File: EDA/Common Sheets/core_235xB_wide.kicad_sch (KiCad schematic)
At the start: 32 parts, among them J4 SM03B-SRSS-TB, J4.1 Conn_01x04, J6 Conn_01x02, SW1 SW_DIP_x04, U1 RP2350_60QFN, U2 W25Q128JVS, Y1 12MHz

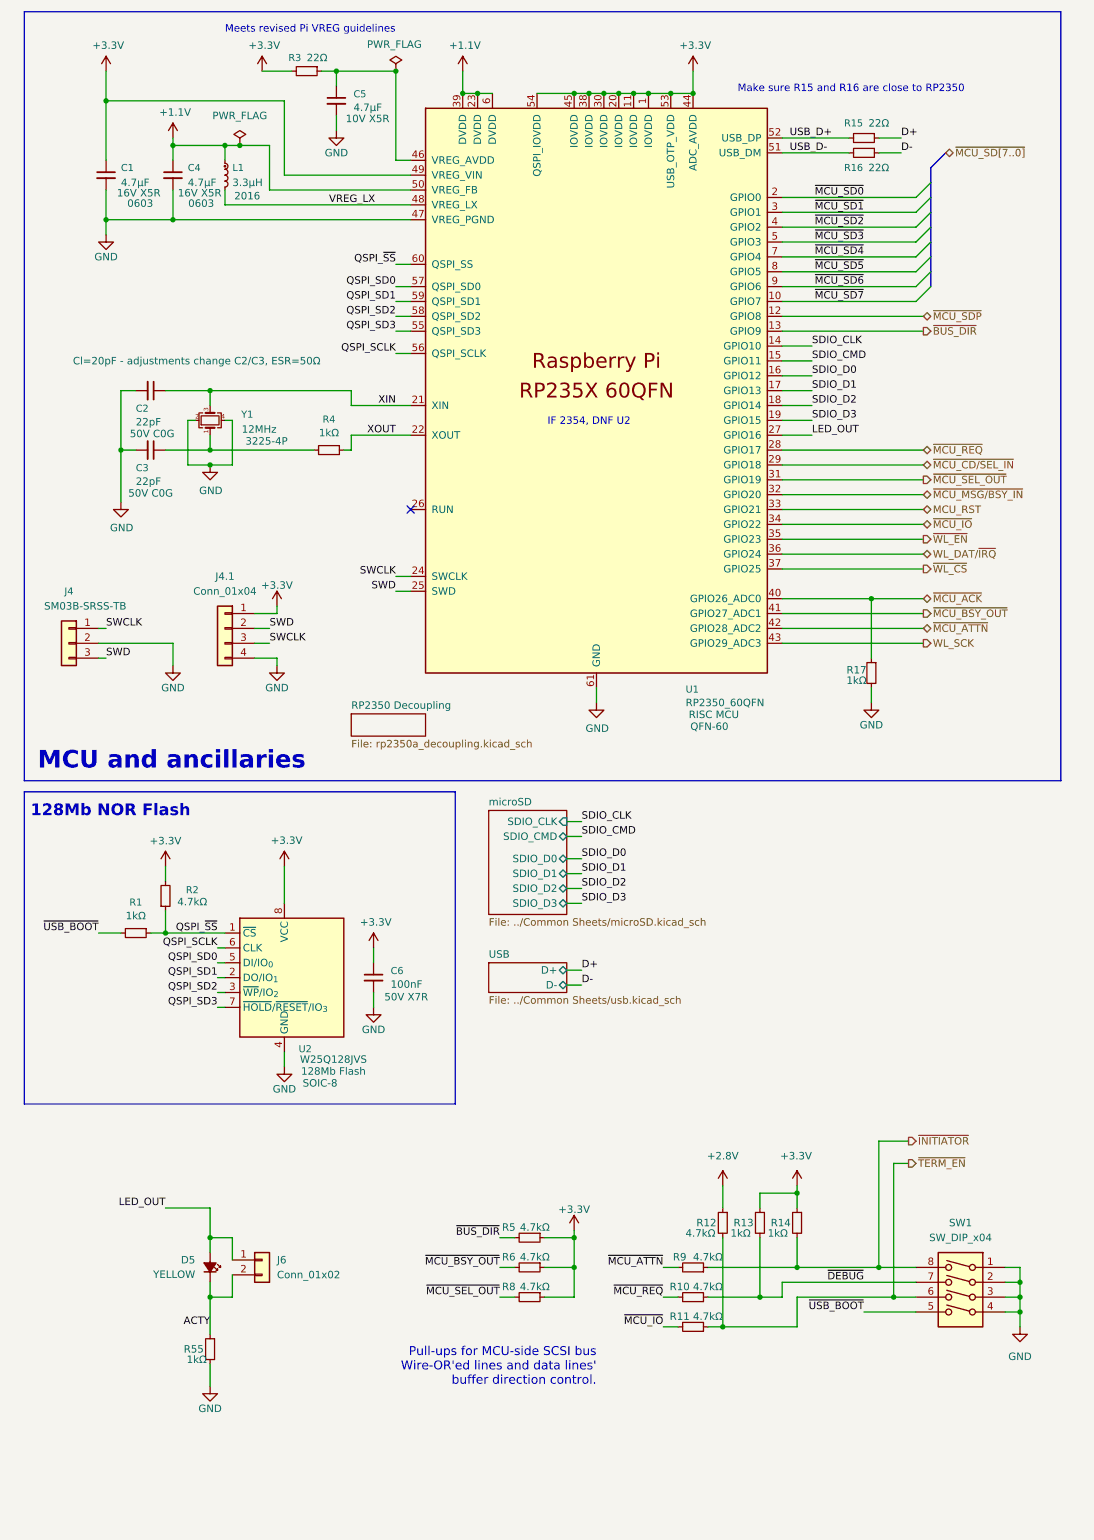
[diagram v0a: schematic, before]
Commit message: Started work on thru-hole SCA wide variant
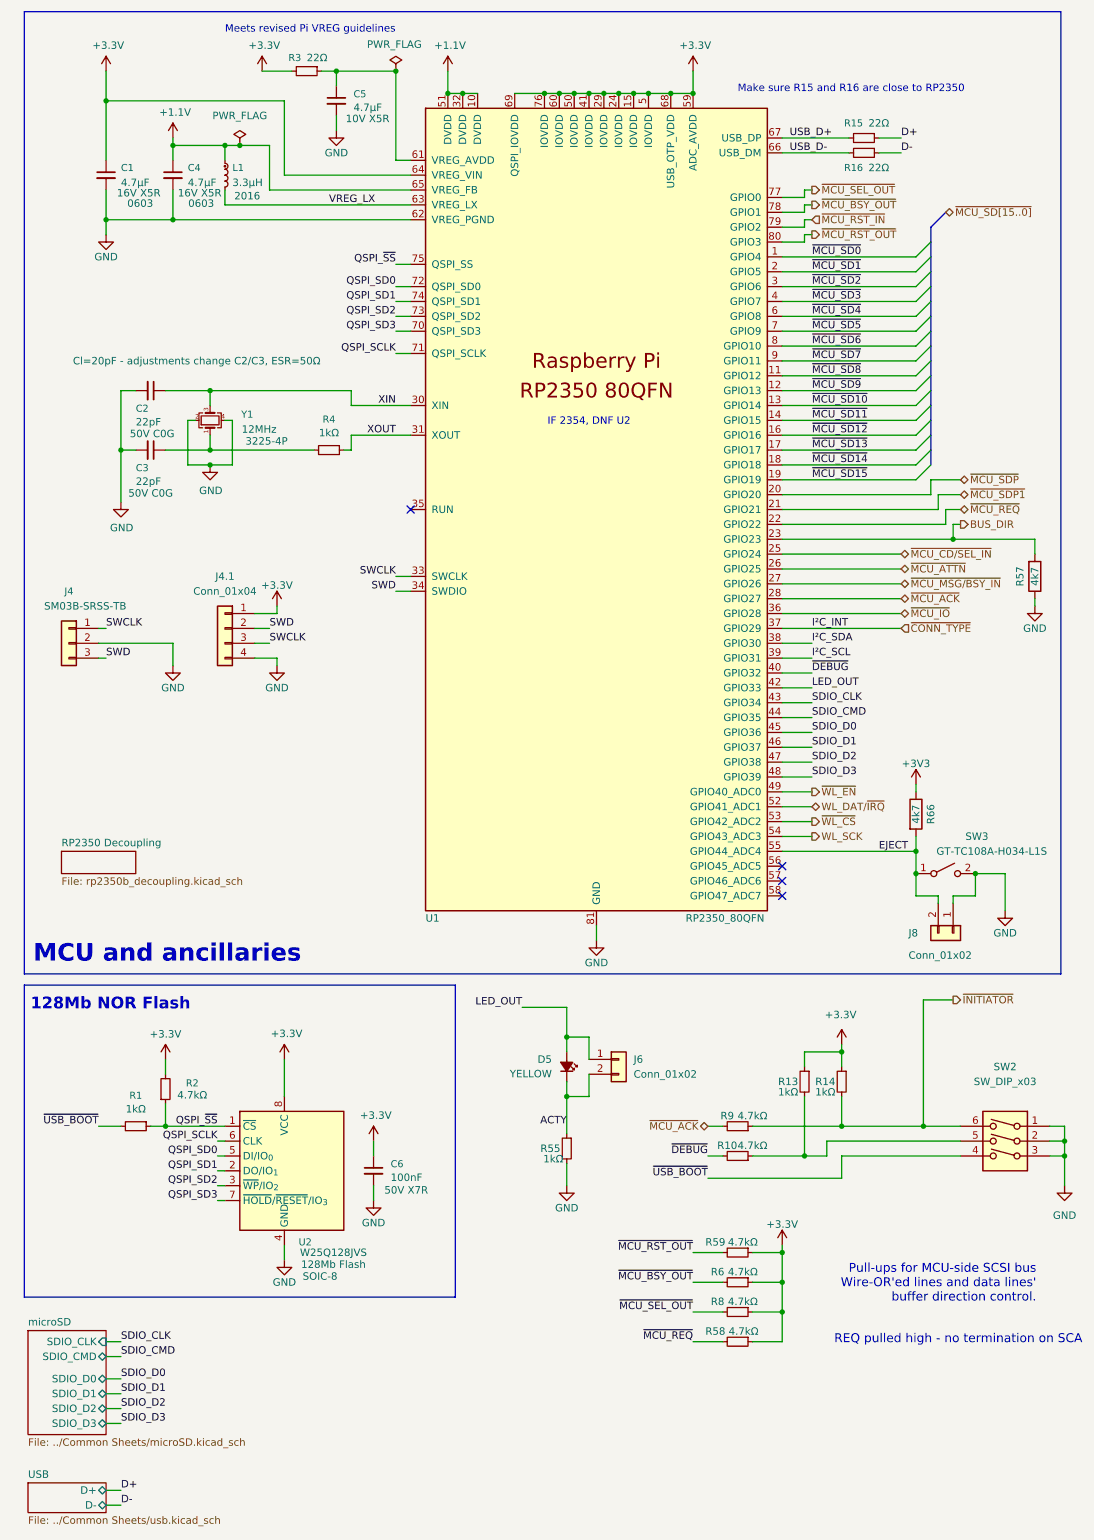
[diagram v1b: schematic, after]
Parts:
- removed R11, R12, R5: 4.7kΩ, Resistor_SMD:R_0603_1608Metric, symbol Device:R_Small
- removed R17: 1kΩ, Resistor_SMD:R_0603_1608Metric, symbol Device:R_Small
- removed SW1: SW_DIP_x04, Button_Switch_SMD:SW_DIP_SPSTx04_Slide_6.7x11.72mm_W8.61mm_P2.54mm_LowProfile, symbol Switch:SW_DIP_x04
- removed U1: RP2350_60QFN, Package_DFN_QFN:QFN-60-1EP_7x7mm_P0.4mm_EP3.4x3.4mm_ThermalVias, symbol GBSCSI:RP2350_60QFN
- added J8: Conn_01x02, Connector_PinHeader_2.54mm:PinHeader_1x02_P2.54mm_Vertical, symbol Connector_Generic:Conn_01x02
- added R57, R66: 4k7, Resistor_SMD:R_0603_1608Metric, symbol Device:R
- added R58, R59: 4.7kΩ, Resistor_SMD:R_0603_1608Metric, symbol Device:R_Small
- added SW2: SW_DIP_x03, Button_Switch_SMD:SW_DIP_SPSTx03_Slide_6.7x9.18mm_W8.61mm_P2.54mm_LowProfile, symbol Switch:SW_DIP_x03
- added SW3: GT-TC108A-H034-L1S, GBSCSI:SW_Push_1P1T-MP_NO_Horizontal_Alps_SKRTLAE010, symbol Switch:SW_SPST
- added U1: RP2350_80QFN, GBSCSI:RP2350-QFN-80-1EP_10x10_P0.4mm_EP3.4x3.4mm_ThermalVias, symbol GBSCSI:RP2350_80QFN
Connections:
- net +1.1V: now also U1.10 (DVDD), U1.32 (DVDD), U1.51 (DVDD), U1.65 (VREG_FB)
- net +3.3V: now also R58.1, R59.1, U1.15 (IOVDD), U1.24 (IOVDD), U1.29 (IOVDD), U1.41 (IOVDD), U1.5 (IOVDD), U1.50 (IOVDD), U1.59 (ADC_AVDD), U1.60 (IOVDD), U1.64 (VREG_VIN), U1.68 (USB_OTP_VDD), U1.69 (QSPI_IOVDD), U1.76 (IOVDD)
- net GND: now also J8.1 (Pin_1), R57.1, SW2.1, SW2.2, SW2.3, SW3.2 (B), U1.62 (VREG_PGND), U1.81 (GND)
- net LED_OUT: now also U1.42 (GPIO33)
- net QSPI_SCLK: now also U1.71 (QSPI_SCLK)
- net QSPI_SD0: now also U1.72 (QSPI_SD0)
- net QSPI_SD1: now also U1.74 (QSPI_SD1)
- net QSPI_SD2: now also U1.73 (QSPI_SD2)
- net QSPI_SD3: now also U1.70 (QSPI_SD3)
- net QSPI_~{SS}: now also U1.75 (QSPI_SS)
- net SDIO_CLK: now also U1.43 (GPIO34)
- net SDIO_CMD: now also U1.44 (GPIO35)
- net SDIO_D0: now also U1.45 (GPIO36)
- net SDIO_D1: now also U1.46 (GPIO37)
- net SDIO_D2: now also U1.47 (GPIO38)
- net SDIO_D3: now also U1.48 (GPIO39)
- net SWCLK: now also U1.33 (SWCLK)
- net SWD: now also U1.34 (SWDIO)
- net USB_D+: now also U1.67 (USB_DP)
- net USB_D-: now also U1.66 (USB_DM)
- net VREG_LX: now also U1.63 (VREG_LX)
- net WL_DAT/~{IRQ}: now also U1.52 (GPIO41_ADC1)
- net WL_SCK: now also U1.54 (GPIO43_ADC3)
- net XIN: now also U1.30 (XIN)
- net XOUT: now also U1.31 (XOUT)
- net ~{DEBUG}: now also R10.2, U1.40 (GPIO32); no longer R10.1, R13.2
- net ~{INITIATOR}: now also SW2.6
- net ~{MCU_ACK}: now also R9.2, U1.28 (GPIO27)
- net ~{MCU_ATTN}: now also U1.26 (GPIO25); no longer R9.2
- net ~{MCU_BSY_OUT}: now also U1.78 (GPIO1)
- net ~{MCU_CD/SEL_IN}: now also U1.25 (GPIO24)
- net ~{MCU_IO}: now also U1.36 (GPIO28)
- net ~{MCU_MSG/BSY_IN}: now also U1.27 (GPIO26)
- net ~{MCU_REQ}: now also R58.2, U1.22 (GPIO22); no longer R10.2
- net ~{MCU_SD0}: now also U1.1 (GPIO4)
- net ~{MCU_SD1}: now also U1.2 (GPIO5)
- net ~{MCU_SD2}: now also U1.3 (GPIO6)
- net ~{MCU_SD3}: now also U1.4 (GPIO7)
- net ~{MCU_SD4}: now also U1.6 (GPIO8)
- net ~{MCU_SD5}: now also U1.7 (GPIO9)
- net ~{MCU_SD6}: now also U1.8 (GPIO10)
- net ~{MCU_SD7}: now also U1.9 (GPIO11)
- net ~{MCU_SDP}: now also U1.20 (GPIO20)
- net ~{MCU_SEL_OUT}: now also U1.77 (GPIO0)
- net ~{USB_BOOT}: now also SW2.4
- net ~{WL_CS}: now also U1.53 (GPIO42_ADC2)
- net ~{WL_EN}: now also U1.49 (GPIO40_ADC0)
- net at C5.1, R3.1: now also U1.61 (VREG_AVDD)
- new net: R10.1, R13.2, SW2.5
- new net +3V3: R66.1
- new net BUS_DIR: R57.2, U1.23 (GPIO23)
- new net EJECT: J8.2 (Pin_2), R66.2, SW3.1 (A), U1.55 (GPIO44_ADC4)
- new net I²C_SCL: U1.39 (GPIO31)
- new net I²C_SDA: U1.38 (GPIO30)
- new net ~{CONN_TYPE}: U1.37 (GPIO29)
- new net ~{MCU_RST_IN}: U1.79 (GPIO2)
- new net ~{MCU_RST_OUT}: R59.2, U1.80 (GPIO3)
- new net ~{MCU_SD10}: U1.13 (GPIO14)
- new net ~{MCU_SD11}: U1.14 (GPIO15)
- new net ~{MCU_SD12}: U1.16 (GPIO16)
- new net ~{MCU_SD13}: U1.17 (GPIO17)
- new net ~{MCU_SD14}: U1.18 (GPIO18)
- new net ~{MCU_SD15}: U1.19 (GPIO19)
- new net ~{MCU_SD8}: U1.11 (GPIO12)
- new net ~{MCU_SD9}: U1.12 (GPIO13)
- new net ~{MCU_SDP1}: U1.21 (GPIO21)
- no-connect marks 1 -> 4
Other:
- sheet RP2350 Decoupling: file rp2350a_decoupling.kicad_sch -> rp2350b_decoupling.kicad_sch
- note added: "REQ pulled high - no termination on SCA"
- moved on the sheet: C6, D5, J6, R1, R10, R13, R14, R2, R55, R6, R8, R9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

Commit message: Fixing up schematics for SCA before layout
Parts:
- R57, R66: value 4k7 -> 4.7kΩ
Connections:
- net +3V3 is gone; now on net +3.3V: R66.1
- net ~{CONN_TYPE} renamed I²C_INT
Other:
- title: GBSCSI2 Common Platform Core - RP235xA, Narrow -> GBSCSI2 Common Platform Core - RP235xB, Wide
- moved on the sheet: R57
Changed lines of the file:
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@@
 	(paper "A4" portrait)
 	(title_block
-		(title "GBSCSI2 Common Platform Core - RP235xA, Narrow")
+		(title "GBSCSI2 Common Platform Core - RP235xB, Wide")
 		(date "2026-02-01")
 		(rev "2.0")
@@
 	(wire
 		(pts
-			(xy 173.99 105.41) (xy 187.96 105.41)
+			(xy 173.99 105.41) (xy 185.42 105.41)
 		)
 		(stroke
@@
 	(wire
 		(pts
-			(xy 149.86 125.73) (xy 144.78 125.73)
+			(xy 165.1 125.73) (xy 144.78 125.73)
 		)
 		(stroke
@@
 	(wire
 		(pts
-			(xy 187.96 116.84) (xy 187.96 115.57)
+			(xy 185.42 116.84) (xy 185.42 115.57)
 		)
 		(stroke
@@
 	(wire
 		(pts
-			(xy 29.21 50.8) (xy 29.21 53.34)
+			(xy 29.21 50.8) (xy 29.21 54.61)
 		)
 		(stroke
@@
 	(wire
 		(pts
-			(xy 187.96 105.41) (xy 187.96 107.95)
+			(xy 185.42 105.41) (xy 185.42 107.95)
 		)
 		(stroke
@@
 	(wire
 		(pts
-			(xy 149.86 123.19) (xy 144.78 123.19)
+			(xy 165.1 123.19) (xy 144.78 123.19)
 		)
 		(stroke
@@
 		)
 	)
-	(label "I²C_INT"
-		(at 149.86 120.65 0)
-		(effects
-			(font
-				(size 1.27 1.27)
-			)
-			(justify left bottom)
-		)
-	)
 	(label "SWCLK"
 		(at 29.21 120.65 0)
@@
 		)
 	)
-	(label "I²C_SDA"
-		(at 149.86 123.19 0)
-		(effects
-			(font
-				(size 1.27 1.27)
-			)
-			(justify left bottom)
-		)
-	)
 	(label "D+"
 		(at 31.75 267.97 0)
@@
 		)
 	)
-	(label "I²C_SCL"
-		(at 149.86 125.73 0)
-		(effects
-			(font
-				(size 1.27 1.27)
-			)
-			(justify left bottom)
-		)
-	)
 	(label "SWD"
 		(at 57.15 120.65 0)
@@
 		)
 	)
+	(hierarchical_label "I²C_INT"
+		(shape input)
+		(at 165.1 120.65 0)
+		(effects
+			(font
+				(size 1.27 1.27)
+			)
+			(justify left)
+		)
+	)
 	(hierarchical_label "~{MCU_BSY_OUT}"
 		(shape output)
@@
 		)
 	)
-	(hierarchical_label "WL_SCK"
+	(hierarchical_label "I²C_SCL"
 		(shape output)
-		(at 149.86 156.21 0)
+		(at 165.1 125.73 0)
 		(effects
 			(font
@@
 		)
 	)
-	(hierarchical_label "~{CONN_TYPE}"
-		(shape input)
-		(at 165.1 120.65 0)
+	(hierarchical_label "WL_SCK"
+		(shape output)
+		(at 149.86 156.21 0)
 		(effects
 			(font
@@
 		)
 	)
+	(hierarchical_label "I²C_SDA"
+		(shape bidirectional)
+		(at 165.1 123.19 0)
+		(effects
+			(font
+				(size 1.27 1.27)
+			)
+			(justify left)
+		)
+	)
 	(hierarchical_label "~{MCU_SD[15..0]}"
 		(shape bidirectional)
@@
 		(dnp no)
 		(property "Reference" "R55"
-			(at 105.156 209.55 0)
+			(at 104.902 209.55 0)
 			(effects
 				(font
@@
 		)
 		(property "Value" "1kΩ"
-			(at 105.664 211.328 0)
+			(at 104.902 211.328 0)
 			(effects
 				(font
@@
 	(symbol
 		(lib_id "power:GND")
-		(at 29.21 53.34 0)
+		(at 29.21 54.61 0)
 		(mirror y)
 		(unit 1)
@@
 		(dnp no)
 		(property "Reference" "#PWR02"
-			(at 29.21 59.69 0)
+			(at 29.21 60.96 0)
 			(effects
 				(font
@@
 		)
 		(property "Value" "GND"
-			(at 29.21 57.15 0)
+			(at 29.21 58.42 0)
 			(effects
 				(font
@@
 		)
 		(property "Footprint" ""
-			(at 29.21 53.34 0)
+			(at 29.21 54.61 0)
 			(effects
 				(font
@@
 		)
 		(property "Datasheet" ""
-			(at 29.21 53.34 0)
+			(at 29.21 54.61 0)
 			(effects
 				(font
@@
 		)
 		(property "Description" ""
-			(at 29.21 53.34 0)
+			(at 29.21 54.61 0)
 			(effects
 				(font
@@
 		(dnp no)
 		(property "Reference" "R66"
-			(at 170.18 152.4 90)
+			(at 171.958 151.13 0)
 			(effects
 				(font
@@
 			)
 		)
-		(property "Value" "4k7"
-			(at 167.64 152.4 90)
+		(property "Value" "4.7kΩ"
+			(at 171.958 153.67 0)
 			(effects
 				(font
@@
 			)
 		)
-		(property "Value" "+3V3"
-			(at 167.64 143.764 0)
+		(property "Value" "+3.3V"
+			(at 167.64 142.24 0)
 			(effects
 				(font
@@
 	(symbol
 		(lib_id "Device:R")
-		(at 187.96 111.76 0)
+		(at 185.42 111.76 0)
 		(mirror x)
 		(unit 1)
@@
 		(dnp no)
 		(property "Reference" "R57"
-			(at 185.42 111.76 90)
+			(at 189.484 110.998 0)
 			(effects
 				(font
@@
 			)
 		)
-		(property "Value" "4k7"
-			(at 187.96 111.76 90)
+		(property "Value" "4.7kΩ"
+			(at 189.484 113.538 0)
 			(effects
 				(font
@@
 		)
 		(property "Footprint" "Resistor_SMD:R_0603_1608Metric"
-			(at 186.182 111.76 90)
+			(at 183.642 111.76 90)
 			(effects
 				(font
@@
 		)
 		(property "Datasheet" ""
-			(at 187.96 111.76 0)
+			(at 185.42 111.76 0)
 			(effects
 				(font
@@
 		)
 		(property "Description" ""
-			(at 187.96 111.76 0)
+			(at 185.42 111.76 0)
 			(effects
 				(font
@@
 		)
 		(property "LCSC" "C23162"
-			(at 187.96 111.76 0)
+			(at 185.42 111.76 0)
 			(effects
 				(font
@@
 		)
 		(property "LCSC Part #" "C23162"
-			(at 187.96 111.76 0)
+			(at 185.42 111.76 0)
 			(effects
 				(font
@@
 	(symbol
 		(lib_id "power:GND")
-		(at 187.96 116.84 0)
+		(at 185.42 116.84 0)
 		(mirror y)
 		(unit 1)
@@
 		(dnp no)
 		(property "Reference" "#PWR025"
-			(at 187.96 123.19 0)
+			(at 185.42 123.19 0)
 			(effects
 				(font
@@
 		)
 		(property "Value" "GND"
-			(at 187.96 120.65 0)
+			(at 185.42 120.65 0)
 			(effects
 				(font
@@
 		)
 		(property "Footprint" ""
-			(at 187.96 116.84 0)
+			(at 185.42 116.84 0)
 			(effects
 				(font
@@
 		)
 		(property "Datasheet" ""
-			(at 187.96 116.84 0)
+			(at 185.42 116.84 0)
 			(effects
 				(font
@@
 		)
 		(property "Description" ""
-			(at 187.96 116.84 0)
+			(at 185.42 116.84 0)
 			(effects
 				(font

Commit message: SCA variant mostly laid out
Or rather, a first pass.
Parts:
- SW3: footprint GBSCSI:SW_Push_1P1T-MP_NO_Horizontal_Alps_SKRTLAE010 -> Button_Switch_SMD:SW_Push_1P1T-MP_NO_Horizontal_Alps_SKRTLAE010
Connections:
- net +3.3V: no longer R58.1, R59.1, R6.1, R8.1
- new net +2.8V: R58.1, R59.1, R6.1, R8.1
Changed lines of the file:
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@@
 			)
 		)
-		(property "Footprint" "GBSCSI:SW_Push_1P1T-MP_NO_Horizontal_Alps_SKRTLAE010"
+		(property "Footprint" "Button_Switch_SMD:SW_Push_1P1T-MP_NO_Horizontal_Alps_SKRTLAE010"
 			(at 172.72 162.56 0)
 			(effects
@@
 	)
 	(symbol
+		(lib_id "power:+2V8")
+		(at 144.78 226.06 0)
+		(unit 1)
+		(exclude_from_sim no)
+		(in_bom yes)
+		(on_board yes)
+		(dnp no)
+		(fields_autoplaced yes)
+		(property "Reference" "#PWR017"
+			(at 144.78 229.87 0)
+			(effects
+				(font
+					(size 1.27 1.27)
+				)
+				(hide yes)
+			)
+		)
+		(property "Value" "+2.8V"
+			(at 144.78 220.98 0)
+			(effects
+				(font
+					(size 1.27 1.27)
+				)
+			)
+		)
+		(property "Footprint" ""
+			(at 144.78 226.06 0)
+			(effects
+				(font
+					(size 1.27 1.27)
+				)
+				(hide yes)
+			)
+		)
+		(property "Datasheet" ""
+			(at 144.78 226.06 0)
+			(effects
+				(font
+					(size 1.27 1.27)
+				)
+				(hide yes)
+			)
+		)
+		(property "Description" ""
+			(at 144.78 226.06 0)
+			(effects
+				(font
+					(size 1.27 1.27)
+				)
+				(hide yes)
+			)
+		)
+		(pin "1"
+		)
+		(instances
+			(project "GBSCSI2_2.5SCA_TH_235x"
+				(path "/93ed3756-682c-4bf3-aa83-42c6b59d82c2/871f9ffd-aa9f-4db2-af7f-735335bcb730"
+					(reference "#PWR017")
+					(unit 1)
+				)
+			)
+		)
+	)
+	(symbol
 		(lib_id "Device:C_Small")
 		(at 40.64 43.18 0)
@@
 					(unit 1)
 				)
-			)
-		)
-	)
-	(symbol
-		(lib_id "power:+3.3V")
-		(at 144.78 226.06 0)
-		(mirror y)
-		(unit 1)
-		(exclude_from_sim no)
-		(in_bom yes)
-		(on_board yes)
-		(dnp no)
-		(property "Reference" "#PWR017"
-			(at 144.78 229.87 0)
-			(effects
-				(font
-					(size 1.27 1.27)
-				)
-				(hide yes)
-			)
-		)
-		(property "Value" "+3.3V"
-			(at 144.78 222.504 0)
-			(effects
-				(font
-					(size 1.27 1.27)
-				)
-			)
-		)
-		(property "Footprint" ""
-			(at 144.78 226.06 0)
-			(effects
-				(font
-					(size 1.27 1.27)
-				)
-				(hide yes)
-			)
-		)
-		(property "Datasheet" ""
-			(at 144.78 226.06 0)
-			(effects
-				(font
-					(size 1.27 1.27)
-				)
-				(hide yes)
-			)
-		)
-		(property "Description" "Power symbol creates a global label with name \"+3.3V\""
-			(at 144.78 226.06 0)
-			(effects
-				(font
-					(size 1.27 1.27)
-				)
-				(hide yes)
-			)
-		)
-		(pin "1"
-		)
-		(instances
-			(project "GBSCSI2_2.5SCA_TH_235x"
-				(path "/93ed3756-682c-4bf3-aa83-42c6b59d82c2/871f9ffd-aa9f-4db2-af7f-735335bcb730"
-					(reference "#PWR017")
-					(unit 1)
-				)
